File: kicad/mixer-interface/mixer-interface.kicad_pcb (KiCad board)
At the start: 2 copper layers, 106.6 x 47 mm, 25 parts, among them J1 PWR_IN, J2 CAN, J3 FAN, Q2 NCEP60T20, U1 AMS1117-5.0, U10 ESP32-DEVKITC-32U, U2 TIME_ENCODER, U3 SPEED_ENCODER, U4 DS18B20, U5 DS18B20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

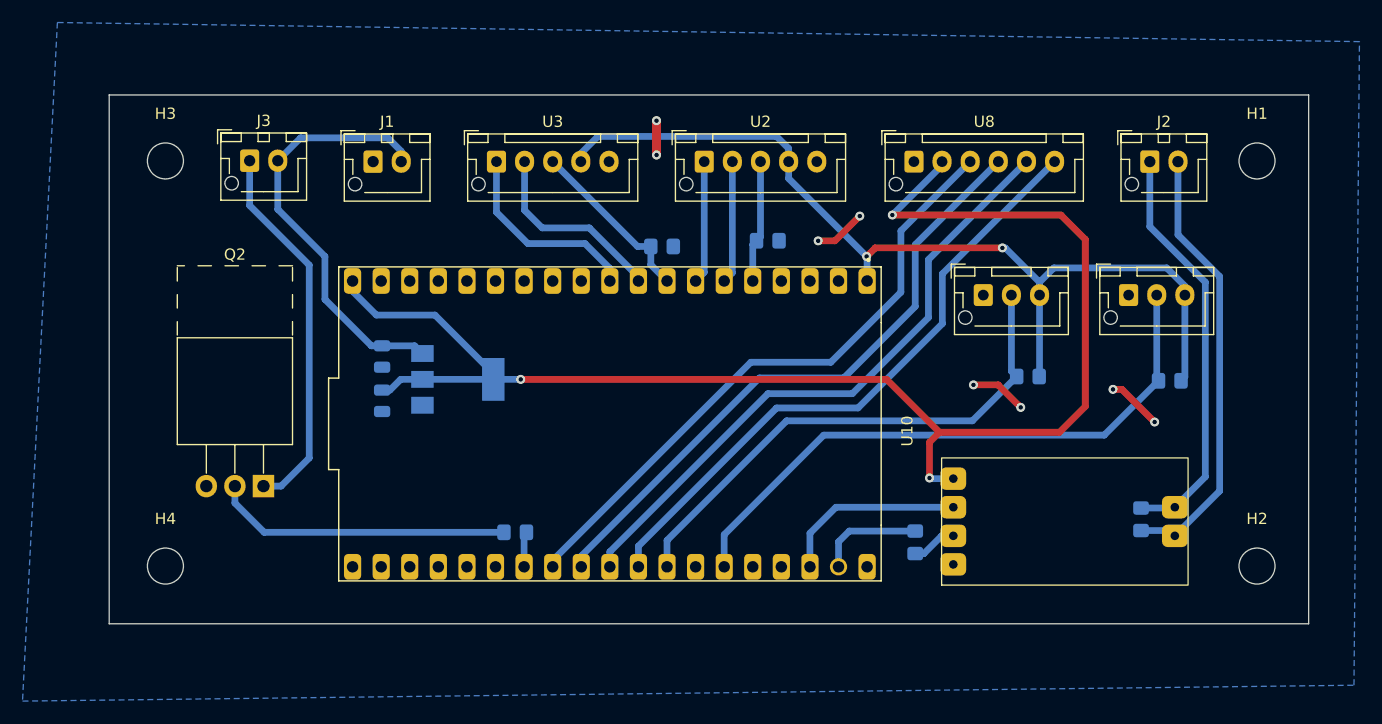
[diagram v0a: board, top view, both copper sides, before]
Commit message: Added encoder breakout and updated other projects
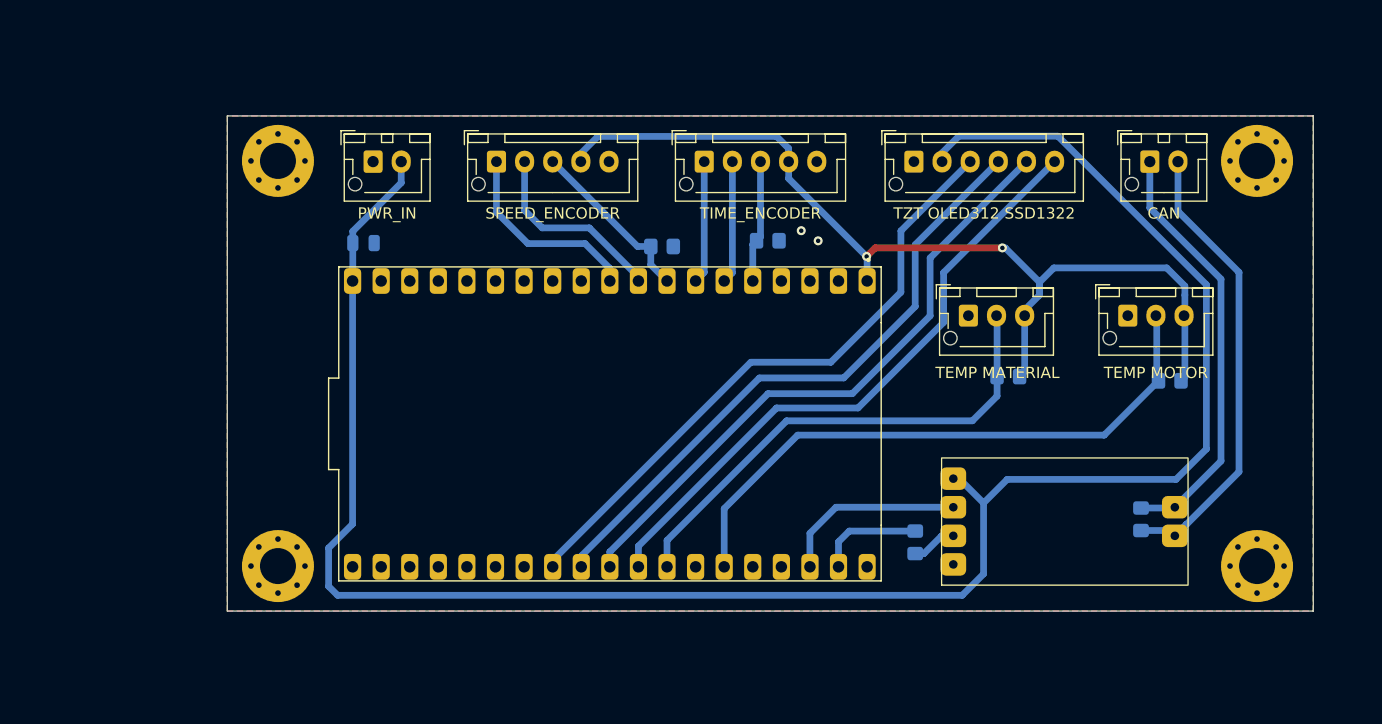
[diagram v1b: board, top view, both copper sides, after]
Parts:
- removed C2, C4: 10u, Capacitor_SMD:C_0805_2012Metric
- removed J3: FAN, Connector_JST:JST_XH_B2B-XH-AM_1x02_P2.50mm_Vertical
- removed Q2: NCEP60T20, --local:TO-220-3_Horizontal_TabUp_no_hole
- removed R7: 1k, Resistor_SMD:R_0805_2012Metric_Pad1.20x1.40mm_HandSolder
- removed U1: AMS1117-5.0, Package_TO_SOT_SMD:SOT-223-3_TabPin2
- added C1: 10u, Capacitor_SMD:C_0805_2012Metric, B.Cu at (62.1, 45.8)
- H1, H2, H3, H4: footprint MountingHole:MountingHole_3.2mm_M3 -> MountingHole:MountingHole_3.2mm_M3_Pad_Via
- U4: value DS18B20 -> TEMP MOTOR
- U5: value DS18B20 -> TEMP MATERIAL
- moved H3 10.0 mm to (54.5, 38.5)
- moved H4 10.0 mm to (54.5, 74.5)
- moved U5 2.26 mm to (115.8, 52.2)
- moved U4 1.83 mm to (130.0, 52.2)
- moved R4 1.74 mm to (119.4, 57.7)
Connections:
- J1 pad 2: +12V -> +5V
- U10 pad 26: /ESP_GPIO_FAN -> unconnected-(U10-IO4-Pad26)
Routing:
- net +5V: track 128.8 -> 176.8 mm, vias 3 -> 0
- net +12V: track 37.9 -> 0.00 mm
- net Net-(J3-Pin_1): track 33.7 -> 0.00 mm
- net Net-(Q2-G): track 26.5 -> 0.00 mm
- net GND: track 17.6 -> 0.00 mm, vias 8 -> 2
- net /ESP_GPIO_FAN: track 3.15 -> 0.00 mm
- net /ESP_1W_T2: track 46.9 -> 44.2 mm
- net /CAN_L: track 39.6 -> 41.1 mm
- net /CAN_H: track 36.9 -> 38.1 mm
- net +3.3V: track 83.9 -> 84.7 mm
- added copper zone on F.Cu, net GND
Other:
- board size 106.6 x 47 mm -> 96.5 x 44 mm

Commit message: Final updates for manufacturing
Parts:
- J1, J2: footprint Connector_JST:JST_XH_B2B-XH-AM_1x02_P2.50mm_Vertical -> Connector_JST:JST_XH_B2B-XH-A_1x02_P2.50mm_Vertical
- U2, U3: footprint Connector_JST:JST_XH_B5B-XH-AM_1x05_P2.50mm_Vertical -> Connector_JST:JST_XH_B5B-XH-A_1x05_P2.50mm_Vertical
- U4, U5: footprint Connector_JST:JST_XH_B3B-XH-AM_1x03_P2.50mm_Vertical -> Connector_JST:JST_XH_B3B-XH-A_1x03_P2.50mm_Vertical
